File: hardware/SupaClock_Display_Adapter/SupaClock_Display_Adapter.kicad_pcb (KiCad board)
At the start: 2 copper layers, 28 x 35 mm, 10 parts, among them J1 Conn_01x08, J2 Conn_01x24, Q1 2N7000

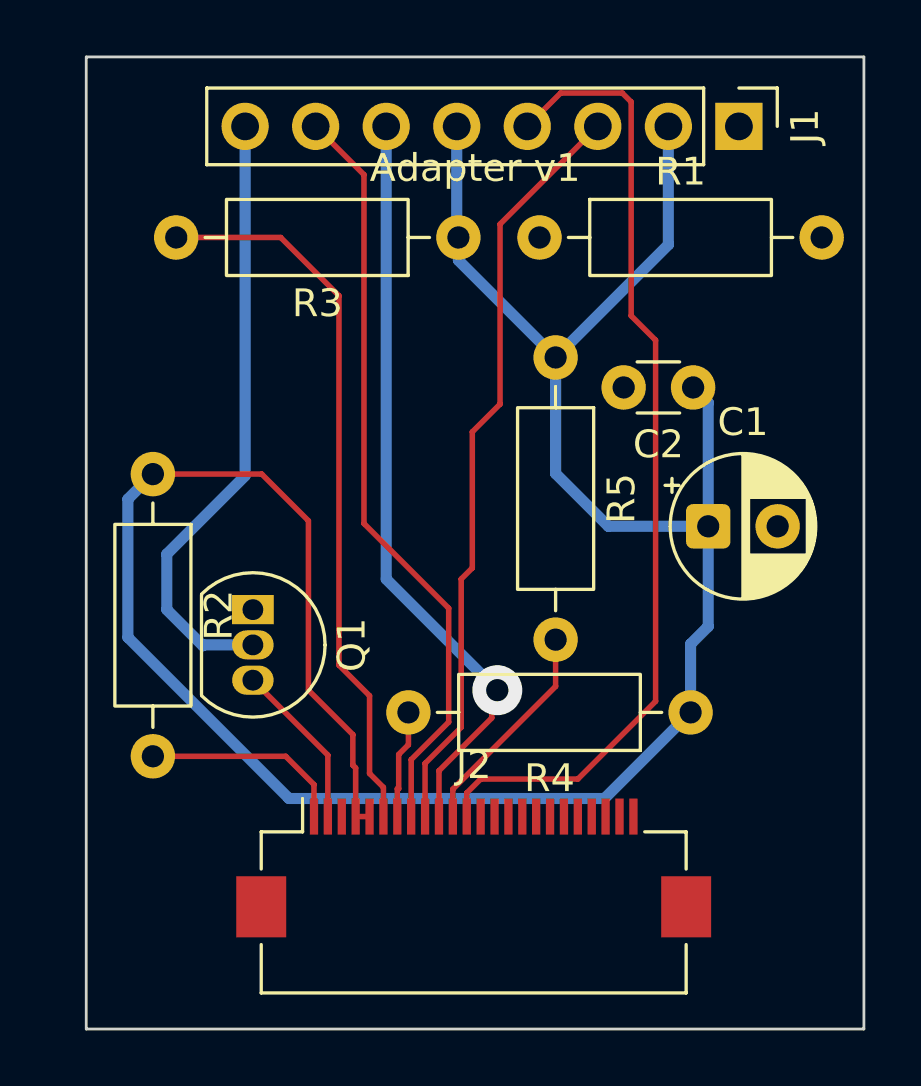
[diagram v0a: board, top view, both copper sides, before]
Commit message: Add new STL file for Supaclock V2 top case
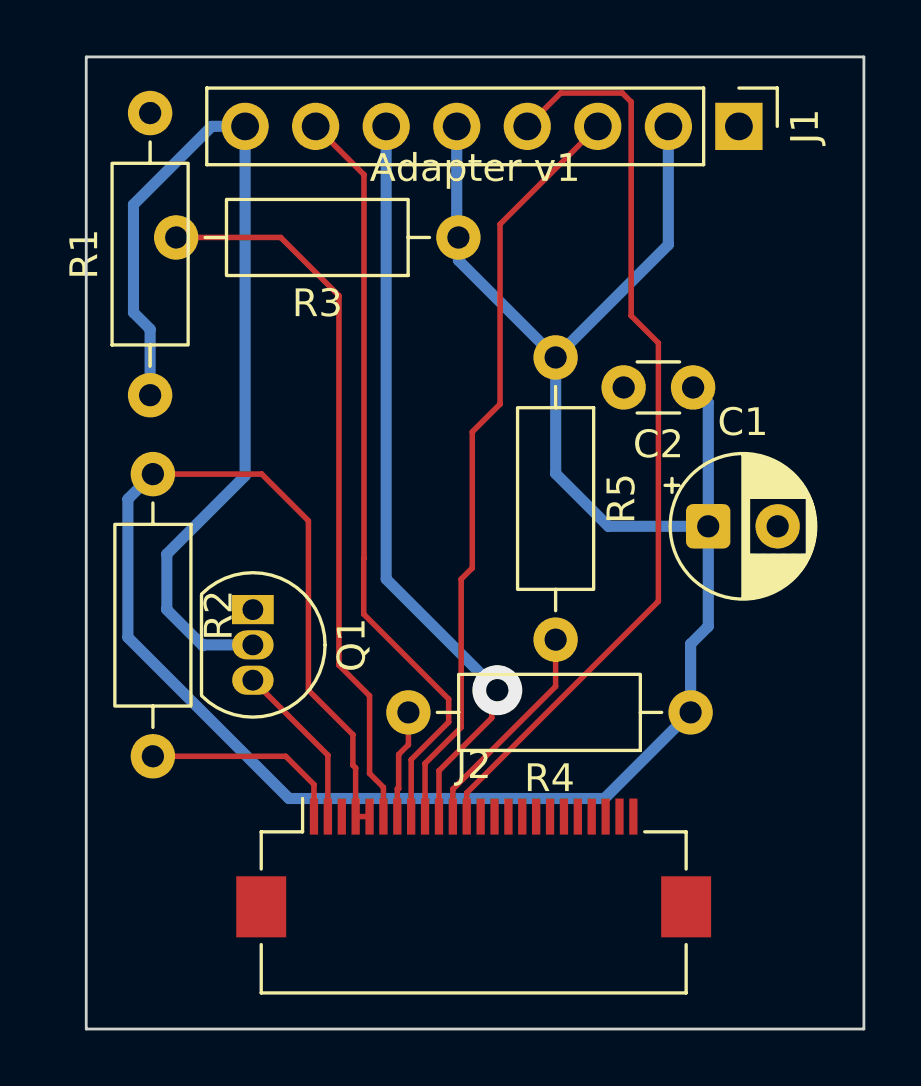
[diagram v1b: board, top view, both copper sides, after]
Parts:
- moved R1 15.1 mm to (38.3, 36.2), turned to 90 degrees
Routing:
- net BLK_PWM: track 22.3 -> 34.6 mm
- net SPI_MOSI: track 35.3 -> 33.4 mm
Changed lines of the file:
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@@
 		(filling no)
 		(pcbplotparams
-			(layerselection 0x00000000_00000000_00000000_007ff7df)
+			(layerselection 0x00000000_00000000_55555555_55555555)
 			(plot_on_all_layers_selection 0x00000000_00000000_00000000_00000000)
 			(disableapertmacros no)
@@
 			(outputformat 1)
 			(mirror no)
-			(drillshape 1)
+			(drillshape 0)
 			(scaleselection 1)
-			(outputdirectory "")
+			(outputdirectory "gerbers/")
 		)
 	)
@@
 	(footprint "Resistor_THT:R_Axial_DIN0207_L6.3mm_D2.5mm_P10.16mm_Horizontal"
 		(layer "F.Cu")
-		(at 52.32 30.5)
+		(at 38.3 36.18 90)
 		(descr "Resistor, Axial_DIN0207 series, Axial, Horizontal, pin pitch=10.16mm, 0.25W = 1/4W, length*diameter=6.3*2.5mm^2, http://cdn-reichelt.de/documents/datenblatt/B400/1_4W%23YAG.pdf")
 		(tags "Resistor Axial_DIN0207 series Axial Horizontal pin pitch 10.16mm 0.25W = 1/4W length 6.3mm diameter 2.5mm")
 		(property "Reference" "R1"
-			(at 5.08 -2.37 0)
+			(at 5.08 -2.37 90)
 			(layer "F.SilkS")
 			(effects
@@
 		)
 		(property "Value" "10k"
-			(at 5.08 2.37 0)
+			(at 5.08 2.37 90)
 			(layer "F.Fab")
 			(effects
@@
 		)
 		(property "Datasheet" ""
-			(at 0 0 0)
+			(at 0 0 90)
 			(layer "F.Fab")
 			(hide yes)
@@
 		)
 		(property "Description" ""
-			(at 0 0 0)
+			(at 0 0 90)
 			(layer "F.Fab")
 			(hide yes)
@@
 		)
 		(property "KiLib_Generator" "resistor/THT"
-			(at 0 0 0)
+			(at 0 0 90)
 			(layer "F.SilkS")
 			(hide yes)
@@
 		(duplicate_pad_numbers_are_jumpers no)
 		(fp_line
-			(start 1.04 0)
-			(end 1.81 0)
+			(start 9.12 0)
+			(end 8.35 0)
 			(stroke
 				(width 0.12)
@@
 		)
 		(fp_line
-			(start 9.12 0)
-			(end 8.35 0)
+			(start 1.04 0)
+			(end 1.81 0)
 			(stroke
 				(width 0.12)
@@
 		)
 		(fp_line
-			(start 0 0)
-			(end 1.93 0)
+			(start 10.16 0)
+			(end 8.23 0)
 			(stroke
 				(width 0.1)
@@
 		)
 		(fp_line
-			(start 10.16 0)
-			(end 8.23 0)
+			(start 0 0)
+			(end 1.93 0)
 			(stroke
 				(width 0.1)
@@
 		)
 		(fp_text user "${REFERENCE}"
-			(at 5.08 0 0)
+			(at 5.08 0 90)
 			(layer "F.Fab")
 			(effects
@@
 		)
 		(pad "1" thru_hole circle
-			(at 0 0)
+			(at 0 0 90)
 			(size 1.6 1.6)
 			(drill 0.8)
@@
 		)
 		(pad "2" thru_hole circle
-			(at 10.16 0)
+			(at 10.16 0 90)
 			(size 1.6 1.6)
 			(drill 0.8)
@@
 	)
 	(segment
+		(start 40.517919 26.5)
+		(end 37.7 29.317919)
+		(width 0.4)
+		(layer "B.Cu")
+		(net "BLK_PWM")
+	)
+	(segment
 		(start 41.72 26.5)
 		(end 41.72 39.08)
@@
 	)
 	(segment
+		(start 37.7 33.2)
+		(end 38.3 33.8)
+		(width 0.4)
+		(layer "B.Cu")
+		(net "BLK_PWM")
+	)
+	(segment
 		(start 40.23 45.17)
 		(end 42 45.17)
@@
 	)
 	(segment
+		(start 41.72 26.5)
+		(end 40.517919 26.5)
+		(width 0.4)
+		(layer "B.Cu")
+		(net "BLK_PWM")
+	)
+	(segment
+		(start 37.7 29.317919)
+		(end 37.7 33.2)
+		(width 0.4)
+		(layer "B.Cu")
+		(net "BLK_PWM")
+	)
+	(segment
 		(start 40.2 45.2)
 		(end 40.23 45.17)
@@
 	)
 	(segment
+		(start 38.3 33.8)
+		(end 38.3 36.18)
+		(width 0.4)
+		(layer "B.Cu")
+		(net "BLK_PWM")
+	)
+	(segment
 		(start 44.7 51.35)
 		(end 44.7 49.14)
@@
 	)
 	(segment
-		(start 49.05 43.85)
-		(end 46 40.8)
+		(start 47.7 51.35)
+		(end 47.7 49.3)
 		(width 0.2)
 		(layer "F.Cu")
@@
 	)
 	(segment
-		(start 46 28.24)
-		(end 44.26 26.5)
+		(start 45.99 42.06)
+		(end 46 42.05)
 		(width 0.2)
 		(layer "F.Cu")
@@
 	)
 	(segment
-		(start 49.05 47.95)
-		(end 49.05 43.85)
+		(start 46 42.05)
+		(end 46 28.24)
 		(width 0.2)
 		(layer "F.Cu")
@@
 	)
 	(segment
-		(start 46 40.8)
-		(end 46 28.24)
+		(start 49.05 47.12)
+		(end 45.99 44.06)
 		(width 0.2)
 		(layer "F.Cu")
@@
 	)
 	(segment
-		(start 47.7 51.35)
-		(end 47.7 49.3)
+		(start 46 28.24)
+		(end 44.26 26.5)
+		(width 0.2)
+		(layer "F.Cu")
+		(net "SPI_CS")
+	)
+	(segment
+		(start 49.05 47.95)
+		(end 49.05 47.12)
+		(width 0.2)
+		(layer "F.Cu")
+		(net "SPI_CS")
+	)
+	(segment
+		(start 45.99 44.06)
+		(end 45.99 42.06)
 		(width 0.2)
 		(layer "F.Cu")
@@
 	)
 	(segment
-		(start 50.2 50)
+		(start 56.6 43.6)
 		(end 49.7 50.5)
 		(width 0.2)
@@
 	(segment
 		(start 55.62 33.32)
-		(end 56.5 34.2)
+		(end 56.6 34.3)
 		(width 0.2)
 		(layer "F.Cu")
@@
 	)
 	(segment
-		(start 53.7 50)
-		(end 50.2 50)
-		(width 0.2)
-		(layer "F.Cu")
-		(net "SPI_MOSI")
-	)
-	(segment
-		(start 55.62 25.62)
-		(end 55.62 33.32)
-		(width 0.2)
-		(layer "F.Cu")
-		(net "SPI_MOSI")
-	)
-	(segment
-		(start 53.08 25.3)
-		(end 55.3 25.3)
+		(start 56.6 34.3)
+		(end 56.6 43.6)
 		(width 0.2)
 		(layer "F.Cu")
@@
 	)
 	(segment
-		(start 56.5 47.2)
-		(end 53.7 50)
+		(start 55.62 25.62)
+		(end 55.62 33.32)
 		(width 0.2)
 		(layer "F.Cu")
@@
 	)
 	(segment
-		(start 56.5 34.2)
-		(end 56.5 47.2)
+		(start 51.88 26.5)
+		(end 53.08 25.3)
 		(width 0.2)
 		(layer "F.Cu")
@@
 	)
 	(segment
-		(start 51.88 26.5)
-		(end 53.08 25.3)
+		(start 53.08 25.3)
+		(end 55.3 25.3)
 		(width 0.2)
 		(layer "F.Cu")
